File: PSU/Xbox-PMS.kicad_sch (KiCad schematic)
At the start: 146 parts, among them IC1 SIC437BED-T1-GE3, IC2 SIC437BED-T1-GE3, IC3 SIC437BED-T1-GE3, IC4 SIC437BED-T1-GE3, IC5 SIC437BED-T1-GE3, SW1 SW_Push, U1 MAX16054, U2 TPS61235PRWLT

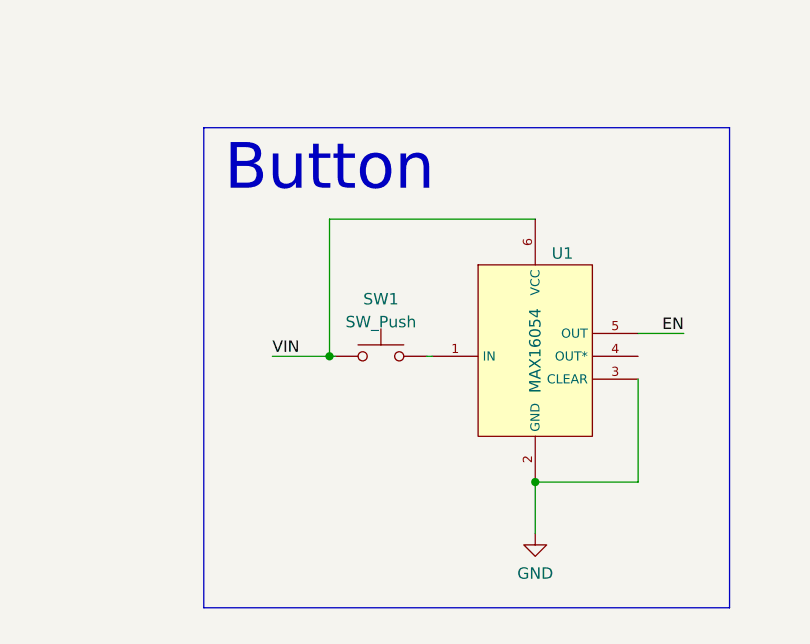
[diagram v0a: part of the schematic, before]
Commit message: Delete HDMI Flipper Design Add HDMI Flex Add USB C/Power and volume button PCB Add Housing CAD Update IDE Flex Update S Controller PCBs Update LPC Flex Update USB Flex
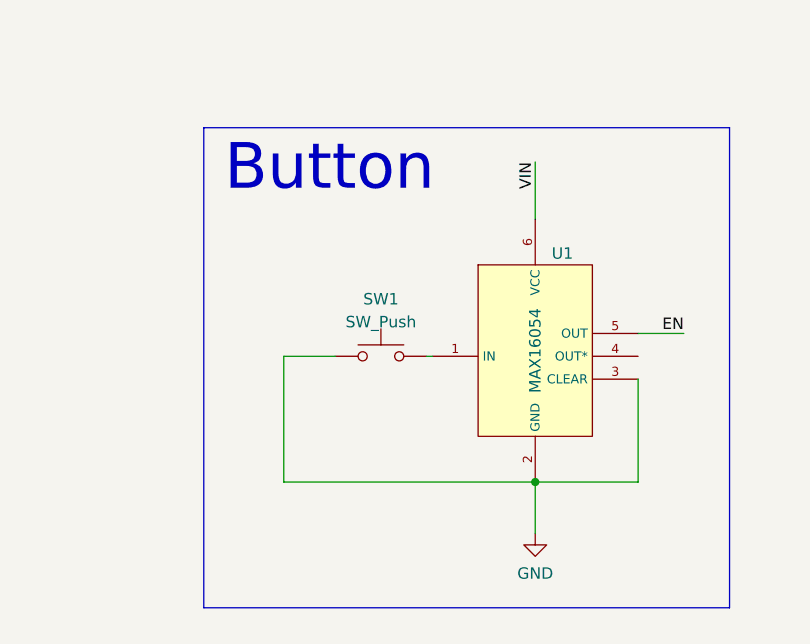
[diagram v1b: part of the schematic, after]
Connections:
- net GND: now also SW1.1
- net VIN: no longer SW1.1
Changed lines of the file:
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@@
 	)
 	(junction
-		(at 386.08 144.78)
-		(diameter 0)
-		(color 0 0 0 0)
-	)
-	(junction
 		(at 153.035 229.87)
 		(diameter 0)
@@
 	(wire
 		(pts
+			(xy 381 144.78) (xy 386.715 144.78)
+		)
+		(stroke
+			(width 0)
+			(type default)
+		)
+	)
+	(wire
+		(pts
 			(xy 406.4 379.73) (xy 406.4 398.145)
 		)
@@
 	(wire
 		(pts
-			(xy 408.94 129.54) (xy 386.08 129.54)
-		)
-		(stroke
-			(width 0)
-			(type default)
-		)
-	)
-	(wire
-		(pts
 			(xy 368.935 365.125) (xy 376.555 365.125)
 		)
@@
 	(wire
 		(pts
-			(xy 379.73 144.78) (xy 386.08 144.78)
+			(xy 408.94 129.54) (xy 408.94 123.19)
 		)
 		(stroke
@@
 	(wire
 		(pts
-			(xy 386.08 129.54) (xy 386.08 144.78)
-		)
-		(stroke
-			(width 0)
-			(type default)
-		)
-	)
-	(wire
-		(pts
 			(xy 351.155 344.805) (xy 354.965 344.805)
 		)
@@
 	(wire
 		(pts
+			(xy 381 158.75) (xy 408.94 158.75)
+		)
+		(stroke
+			(width 0)
+			(type default)
+		)
+	)
+	(wire
+		(pts
 			(xy 106.68 316.865) (xy 106.68 318.77)
 		)
@@
 	(wire
 		(pts
-			(xy 386.08 144.78) (xy 386.715 144.78)
-		)
-		(stroke
-			(width 0)
-			(type default)
-		)
-	)
-	(wire
-		(pts
 			(xy 274.955 274.955) (xy 330.2 274.955)
 		)
@@
 	(wire
 		(pts
+			(xy 381 144.78) (xy 381 158.75)
+		)
+		(stroke
+			(width 0)
+			(type default)
+		)
+	)
+	(wire
+		(pts
 			(xy 92.075 358.14) (xy 97.79 358.14)
 		)
@@
 	)
 	(label "VIN"
-		(at 379.73 144.78 0)
+		(at 408.94 123.19 270)
 		(fields_autoplaced yes)
 		(effects
@@
 				(size 1.27 1.27)
 			)
-			(justify left bottom)
+			(justify right bottom)
 		)
 	)
